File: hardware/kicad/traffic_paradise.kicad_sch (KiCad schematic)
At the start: 58 parts, among them J2 USB C, Q1 SS8050, Q2 SS8050, SW1 SW_Push, SW2 SW_Push, SW3 SW_Push, U1 ESP32-WROOM-32, U2 AMS1117-3.3, U3 USBLC6-2SC6, U4 CP2102N-A02-GQFN28

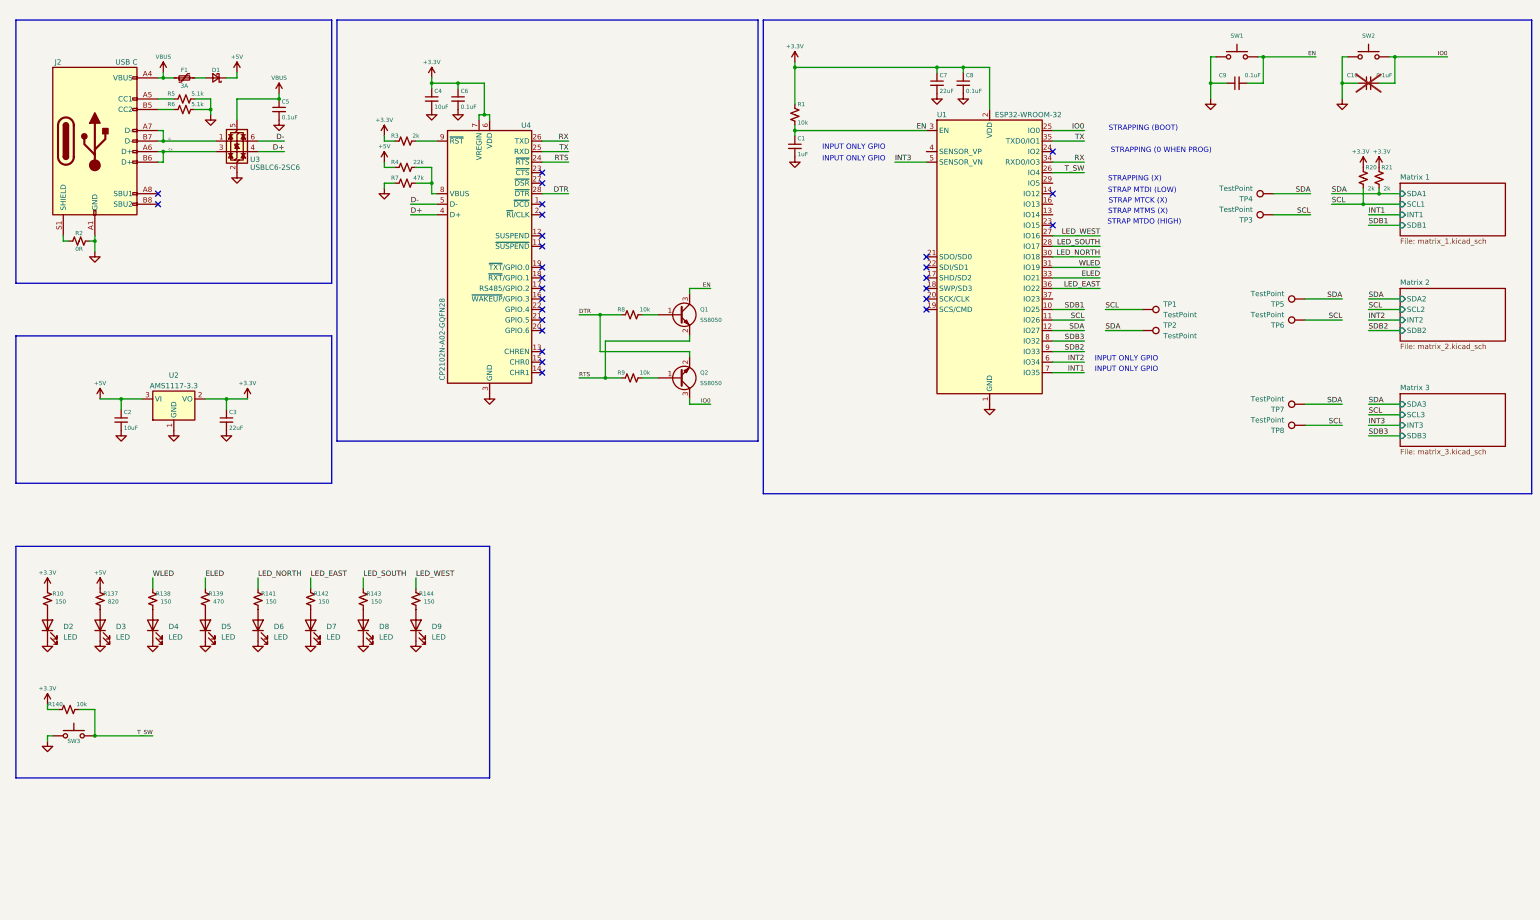
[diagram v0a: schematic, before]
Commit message: add jtag functionality with tristate buffers
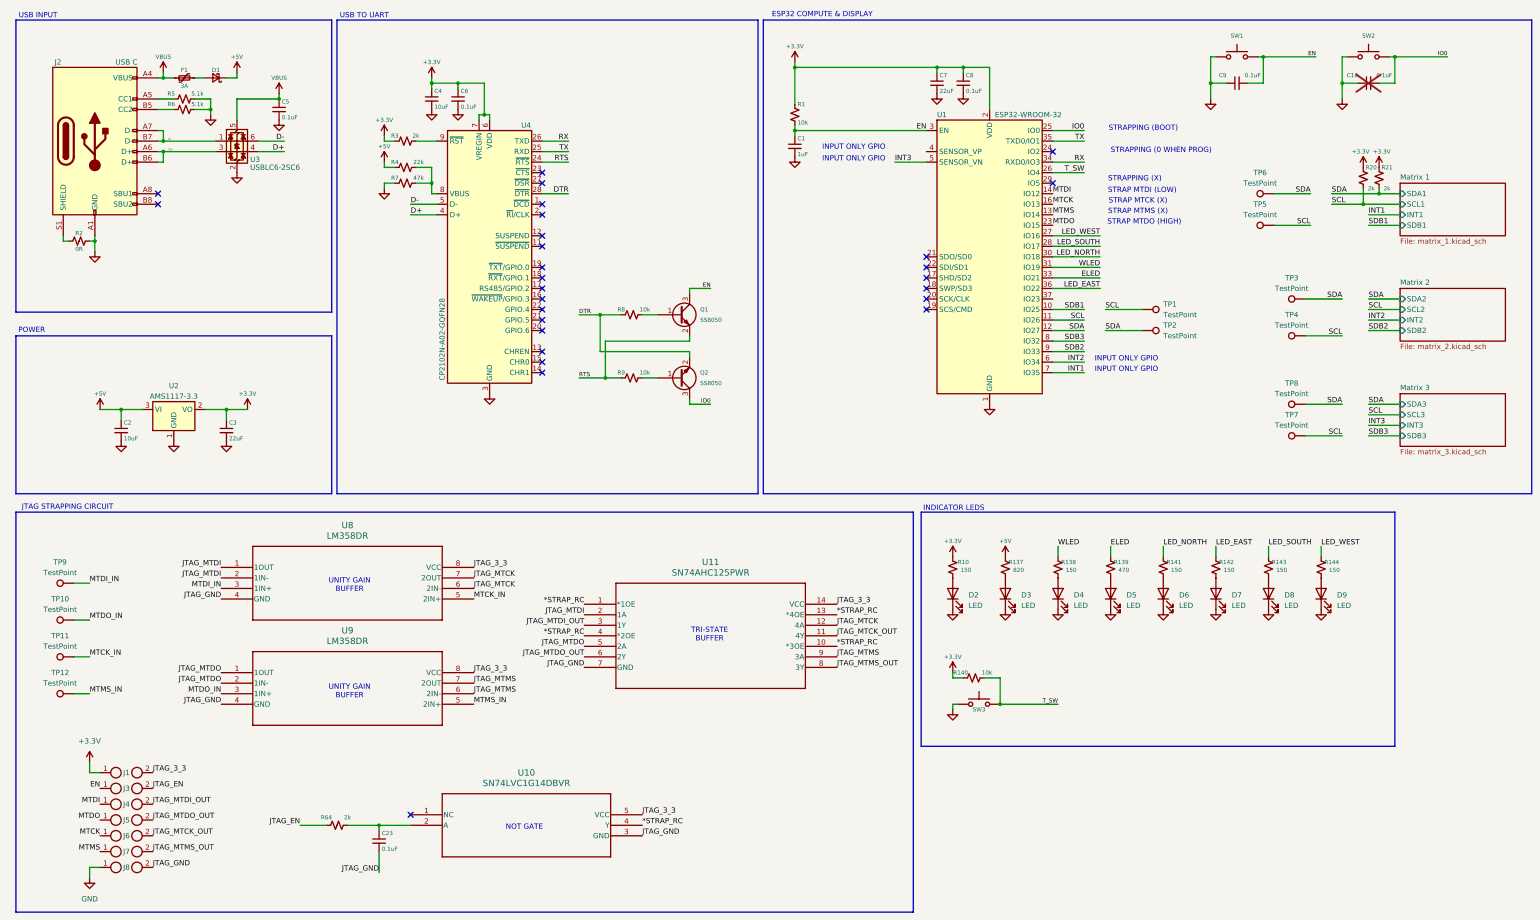
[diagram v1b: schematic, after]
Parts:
- added C23: 0.1uF, Capacitor_SMD:C_0402_1005Metric, symbol Device:C_Small
- added J1, J3, J4, J5, J6, J7, J8: ~, jumpers:breadboard_jumper, symbol Isolators:breadboard_jumper
- added R64: 2k, Resistor_SMD:R_0402_1005Metric, symbol Device:R_Small_US
- added TP10, TP11, TP12, TP9: TestPoint, TestPoint:TestPoint_THTPad_2.5x2.5mm_Drill1.2mm, symbol Connector:TestPoint
- added U10: SN74LVC1G14DBVR, map_lbr:DBV5, symbol SN74LVC1G14DBVR:SN74LVC1G14DBVR
- added U11: SN74AHC125PWR, map_lbr:PW14, symbol SN74AHC125PWR:SN74AHC125PWR
- added U8, U9: LM358DR, map_lbr:D8, symbol LM358DR:LM358DR
- TP1, TP2, TP3, TP4, TP5, TP6, TP7, TP8: footprint TestPoint:TestPoint_THTPad_1.5x1.5mm_Drill0.7mm -> TestPoint:TestPoint_THTPad_2.5x2.5mm_Drill1.2mm
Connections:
- net +3.3V: now also J1.1
- net EN: now also J3.1
- net GND: now also J8.1
- net SCL: now also TP4.1, TP5.1, TP7.1; no longer TP3.1, TP6.1, TP8.1
- net SDA: now also TP3.1, TP6.1, TP8.1; no longer TP4.1, TP5.1, TP7.1
- net MTMS: now reaches U1.13 (IO14)
- net MTMS: now also J7.1
- net MTDI: now reaches U1.14 (IO12)
- net MTDI: now also J4.1
- net MTCK: now reaches U1.16 (IO13)
- net MTCK: now also J6.1
- net MTDO: now reaches U1.23 (IO15)
- net MTDO: now also J5.1
- new net: C23.1, R64.2, U10.2 (A)
- new net *STRAP_RC: U10.4 (Y), U11.1 (*1OE), U11.10 (*3OE), U11.13 (*4OE), U11.4 (*2OE)
- new net JTAG_3_3: J1.2, U10.5 (VCC), U11.14 (VCC), U8.8 (VCC), U9.8 (VCC)
- new net JTAG_EN: J3.2, R64.1
- new net JTAG_GND: C23.2, J8.2, U10.3 (GND), U11.7 (GND), U8.4 (GND), U9.4 (GND)
- new net JTAG_MTCK: U11.12 (4A), U8.6 (2IN-), U8.7 (2OUT)
- new net JTAG_MTCK_OUT: J6.2, U11.11 (4Y)
- new net JTAG_MTDI: U11.2 (1A), U8.1 (1OUT), U8.2 (1IN-)
- new net JTAG_MTDI_OUT: J4.2, U11.3 (1Y)
- new net JTAG_MTDO: U11.5 (2A), U9.1 (1OUT), U9.2 (1IN-)
- new net JTAG_MTDO_OUT: J5.2, U11.6 (2Y)
- new net JTAG_MTMS: U11.9 (3A), U9.6 (2IN-), U9.7 (2OUT)
- new net JTAG_MTMS_OUT: J7.2, U11.8 (3Y)
- new net MTCK_IN: TP11.1, U8.5 (2IN+)
- new net MTDI_IN: TP9.1, U8.3 (1IN+)
- new net MTDO_IN: TP10.1, U9.3 (1IN+)
- new net MTMS_IN: TP12.1, U9.5 (2IN+)
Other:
- note added: "ESP32 COMPUTE & DISPLAY"
- note added: "INDICATOR LEDS"
- note added: "JTAG STRAPPING CIRCUIT"
- note added: "NOT GATE"
- note added: "POWER"
- note added: "TRI-STATE BUFFER"
- note added: "UNITY GAIN BUFFER"
- note added: "USB INPUT"
- note added: "USB TO UART"
- moved on the sheet: C2, C3, D2, D3, D4, D5, D6, D7, D8, D9, R10, R137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

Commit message: changed test points/jumpers, some other changes
also added photoresistor connected to pin 4 (ADC1) and slightly changed some silkscreen
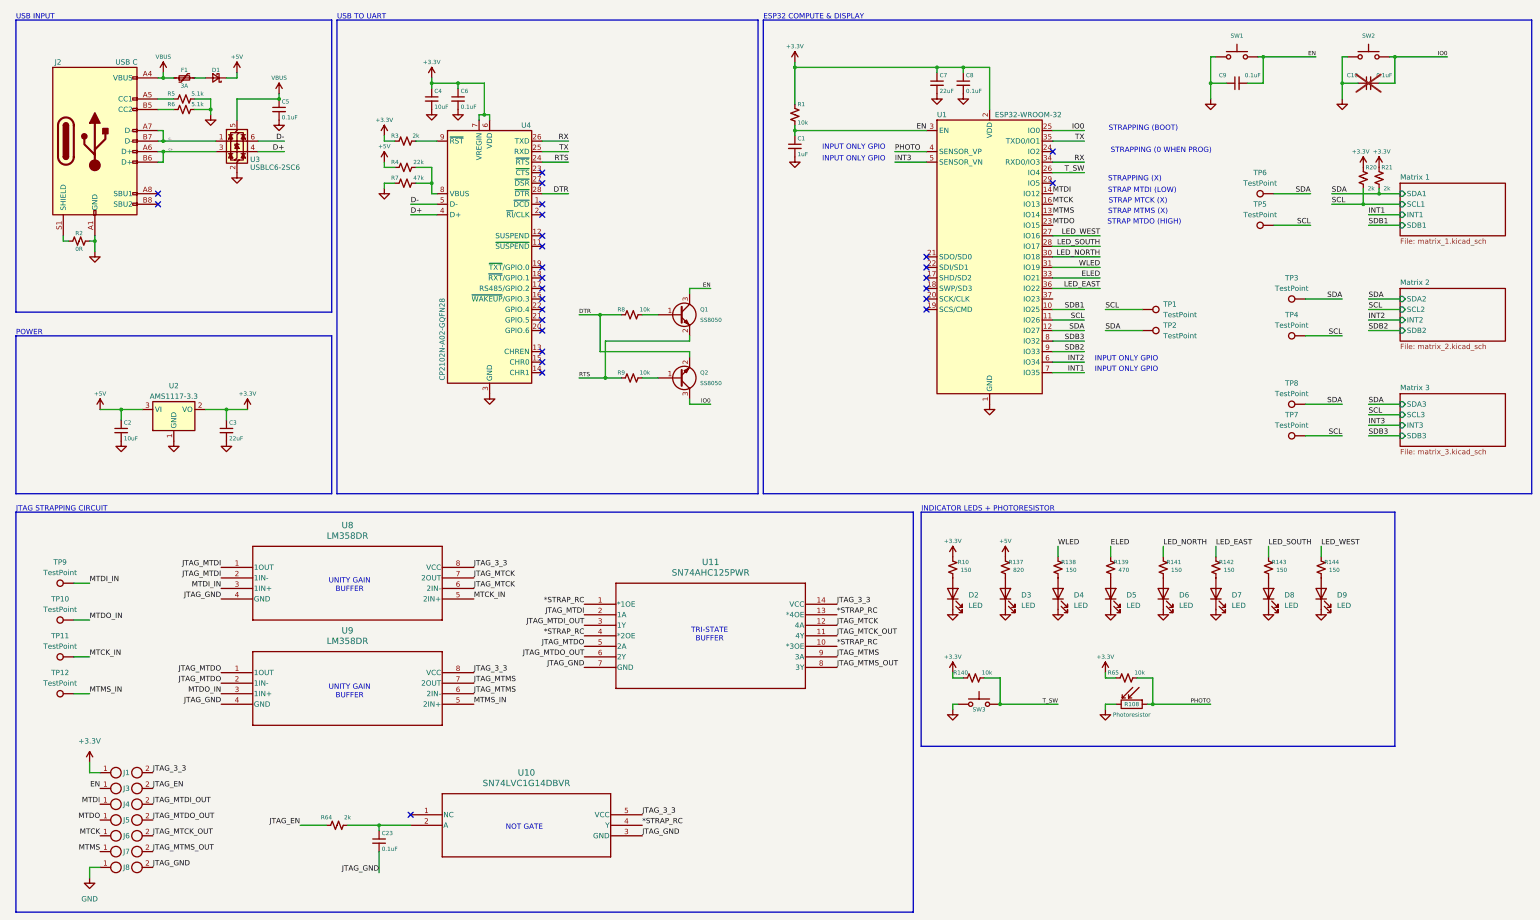
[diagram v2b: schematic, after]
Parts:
- added R108: Photoresistor, map_lbr:Photoresistor, symbol Device:R_Photo
- added R65: 10k, Resistor_SMD:R_0402_1005Metric, symbol Device:R_Small_US
- J1, J3, J4, J5, J6, J7, J8: footprint jumpers:breadboard_jumper -> Jumper:SolderJumper-2_P1.3mm_Open_TrianglePad1.0x1.5mm
- TP1, TP2, TP3, TP4, TP5, TP6, TP7, TP8: footprint TestPoint:TestPoint_THTPad_2.5x2.5mm_Drill1.2mm -> TestPoint:TestPoint_Pad_D2.5mm
- TP10, TP11, TP12, TP9: footprint TestPoint:TestPoint_THTPad_2.5x2.5mm_Drill1.2mm -> TestPoint:TestPoint_THTPad_D2.0mm_Drill1.0mm
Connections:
- net +3.3V: now also R65.1
- net GND: now also R108.2
- net PHOTO: now reaches U1.4 (SENSOR_VP)
- net PHOTO: now also R108.1, R65.2
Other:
- note added: "INDICATOR LEDS + PHOTORESISTOR"
- note removed: "INDICATOR LEDS"

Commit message: Added LED key, update LED, some other changes
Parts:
- added C24: 0.1uF, Capacitor_SMD:C_0402_1005Metric, symbol Device:C_Small
- TP10, TP11, TP12, TP9: footprint TestPoint:TestPoint_THTPad_D2.0mm_Drill1.0mm -> TestPoint:TestPoint_Pad_D2.5mm
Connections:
- net GND: now also C24.1
- net PHOTO: now also C24.2
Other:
- moved on the sheet: R108, R140, R65, SW3

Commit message: add power wall mount
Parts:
- added TP21, TP22: TestPoint, TestPoint:TestPoint_Pad_D2.5mm, symbol Connector:TestPoint
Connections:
- net GND: now also TP21.1
- net VBUS: now also TP22.1
- net CC1: now reaches J2.A5 (CC1), R5.1
- net CC2: now reaches J2.B5 (CC2), R6.1
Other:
- moved on the sheet: R5, R6

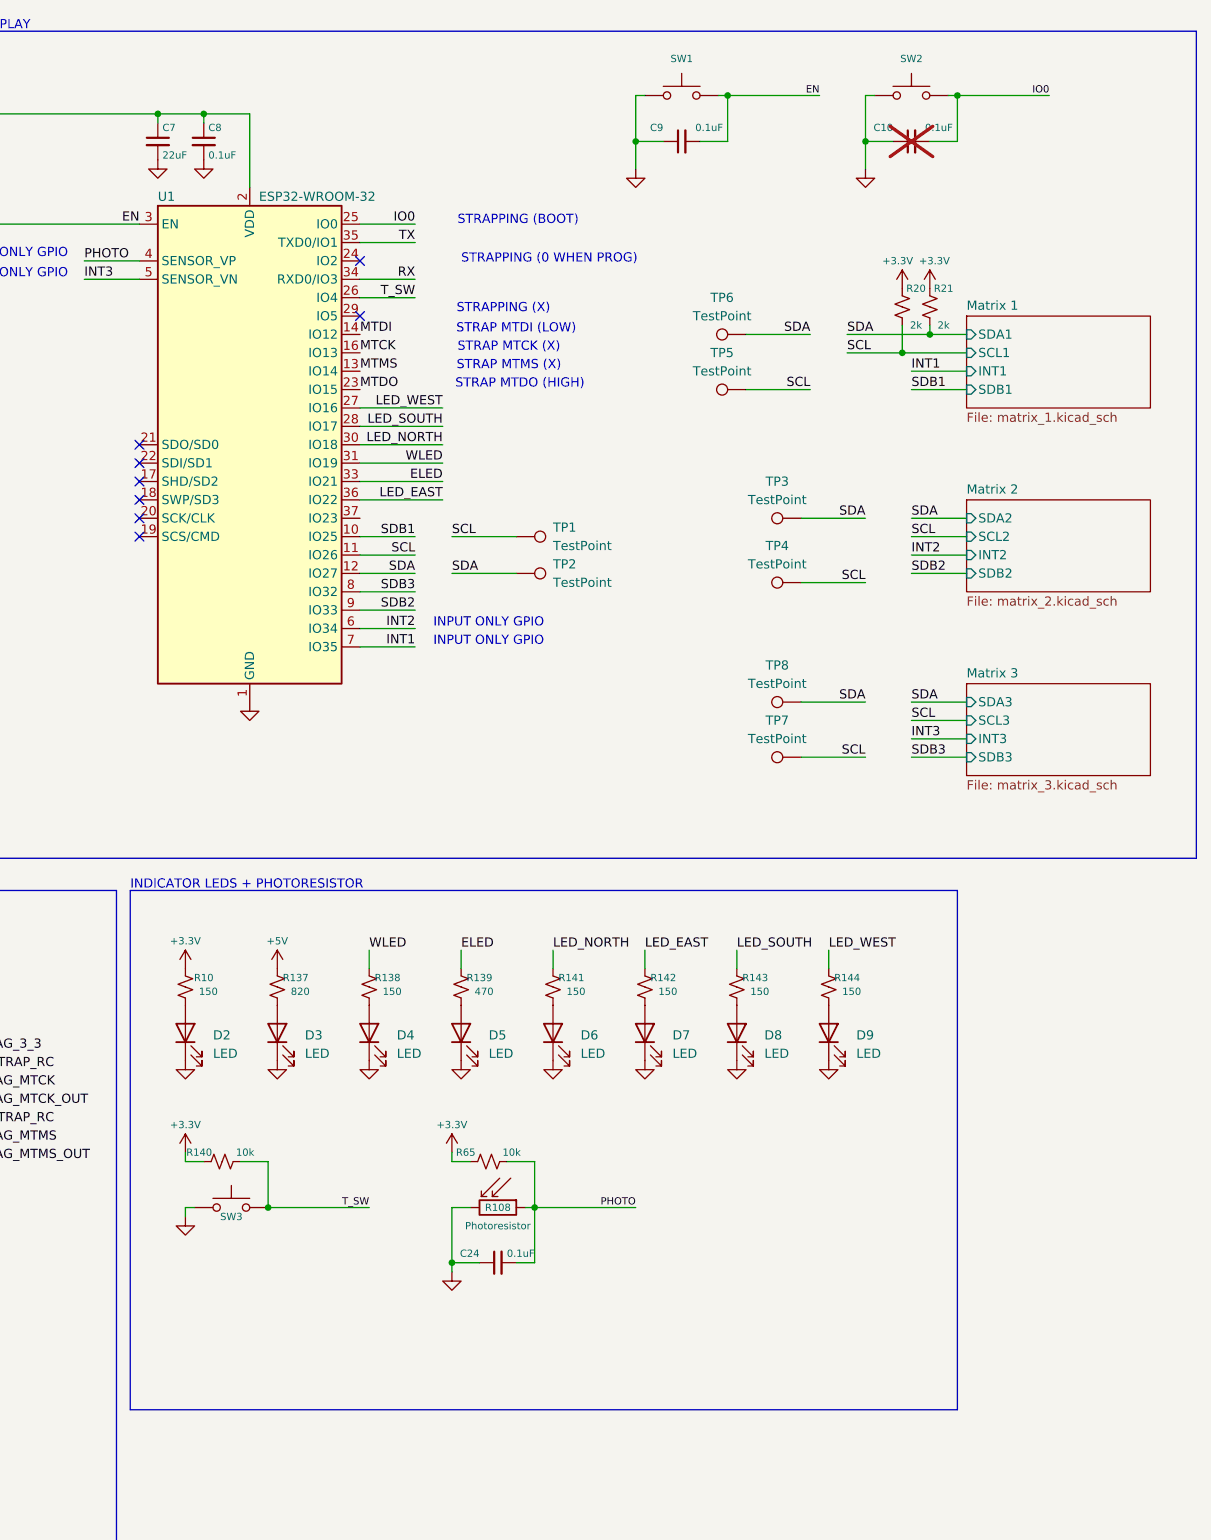
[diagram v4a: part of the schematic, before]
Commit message: add and route matrix 4
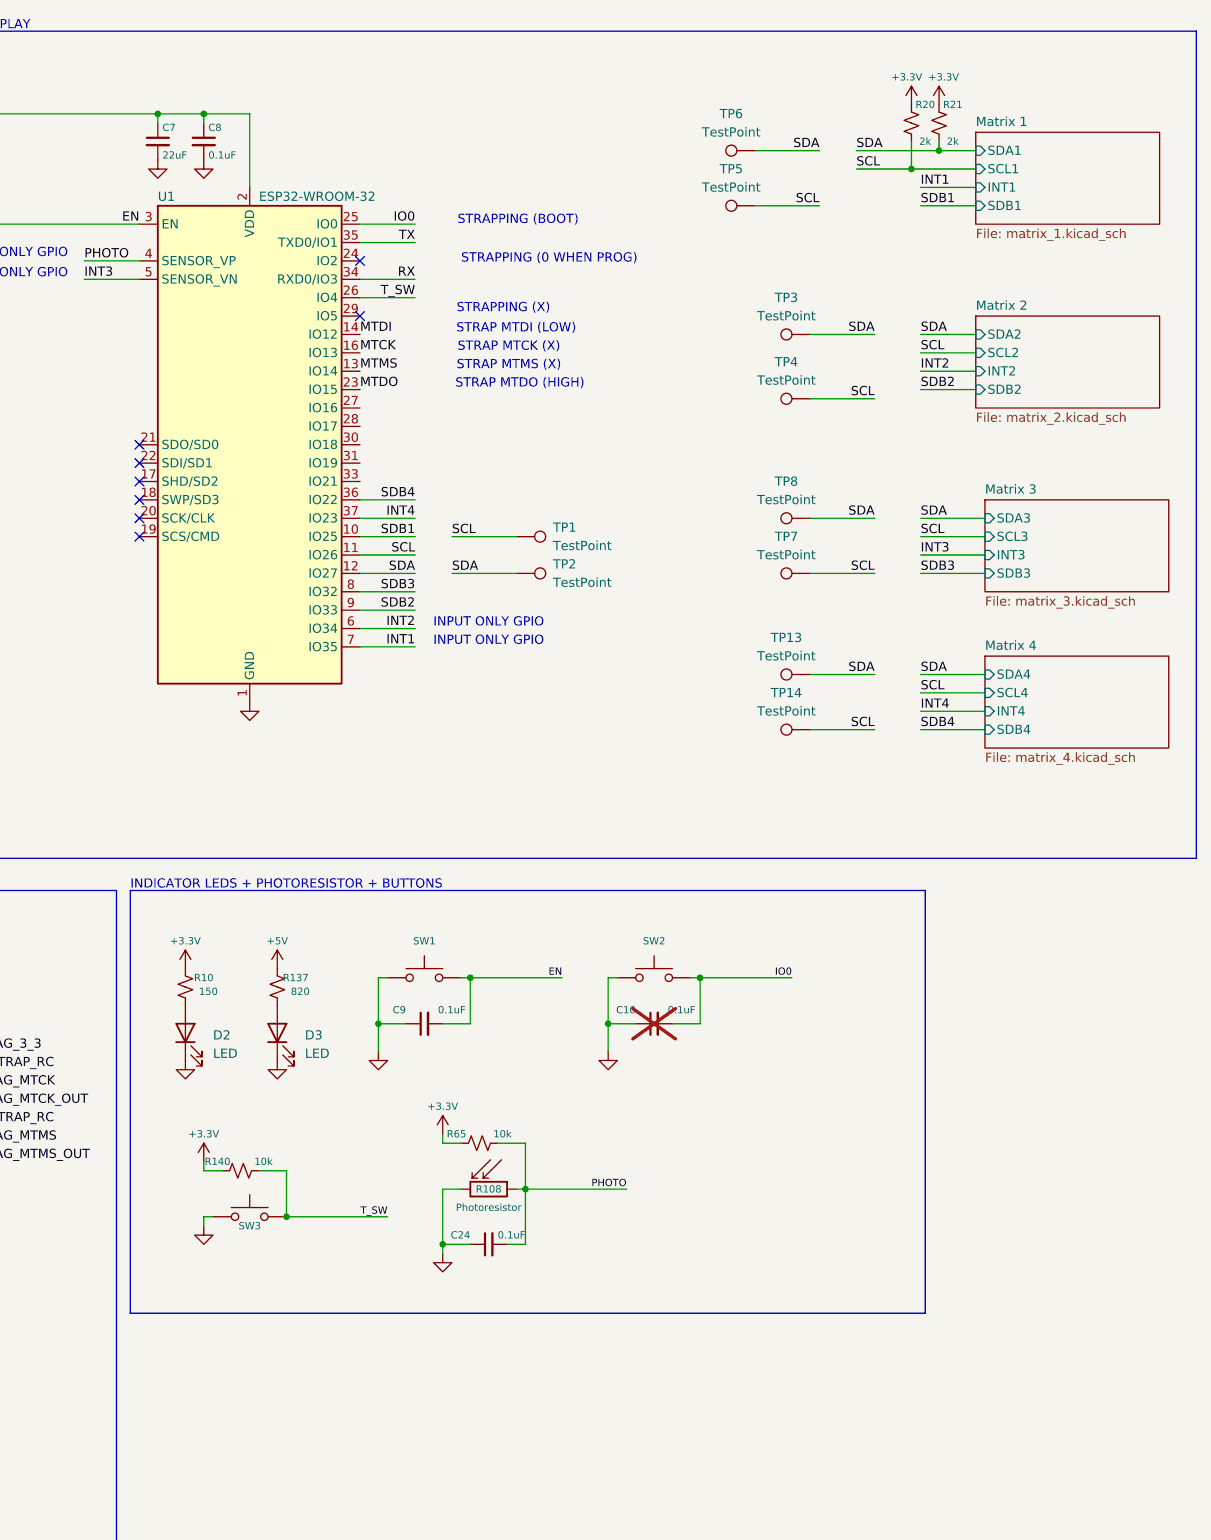
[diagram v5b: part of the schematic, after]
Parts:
- removed D4, D5: LED, LED_SMD:LED_0805_2012Metric, symbol Device:LED
- removed D6, D7, D8, D9: LED, map_lbr:LED_0805_2012Metric_Clean, symbol Device:LED
- removed R138, R141, R142, R143, R144: 150, Resistor_SMD:R_0603_1608Metric, symbol Device:R_Small_US
- removed R139: 470, Resistor_SMD:R_0402_1005Metric, symbol Device:R_Small_US
- added TP13, TP14: TestPoint, TestPoint:TestPoint_Pad_D2.5mm, symbol Connector:TestPoint
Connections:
- net SCL: now also TP14.1
- net SDA: now also TP13.1
- net INT4: now reaches U1.37 (IO23)
- net ELED: no longer names the net of U1.33 (IO21)
- net LED_EAST renamed SDB4
- net LED_NORTH: no longer names the net of U1.30 (IO18)
- net LED_SOUTH: no longer names the net of U1.28 (IO17)
- net LED_WEST: no longer names the net of U1.27 (IO16)
- net WLED: no longer names the net of U1.31 (IO19)
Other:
- added sheet Matrix 4 (matrix_4.kicad_sch)
- note added: "INDICATOR LEDS + PHOTORESISTOR + BUTTONS"
- note removed: "INDICATOR LEDS + PHOTORESISTOR"
- moved on the sheet: C10, C24, C9, R108, R140, R20, R21, R65, SW1, SW2, SW3, TP3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
